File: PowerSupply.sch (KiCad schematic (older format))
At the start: 22 parts, among them IC1 TPS61252DSGT, J6 Conn_01x02, U1 LM27762

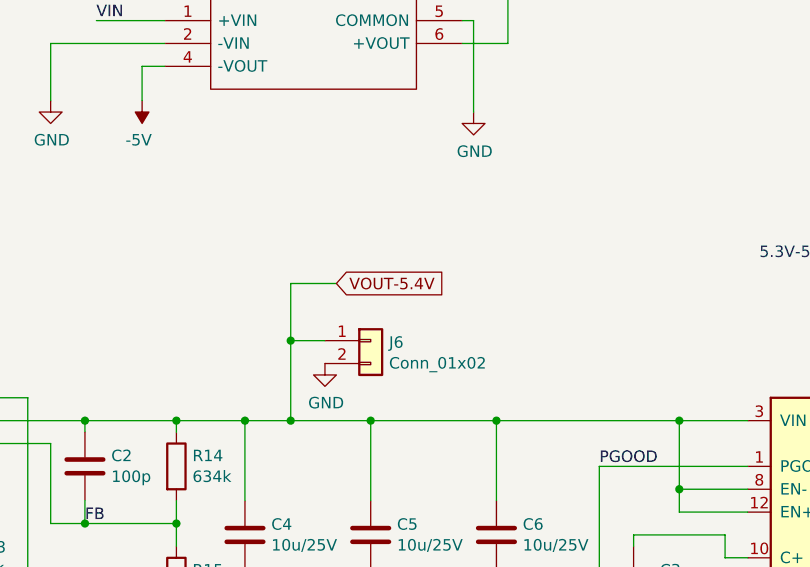
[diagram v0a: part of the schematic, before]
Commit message: larger conn
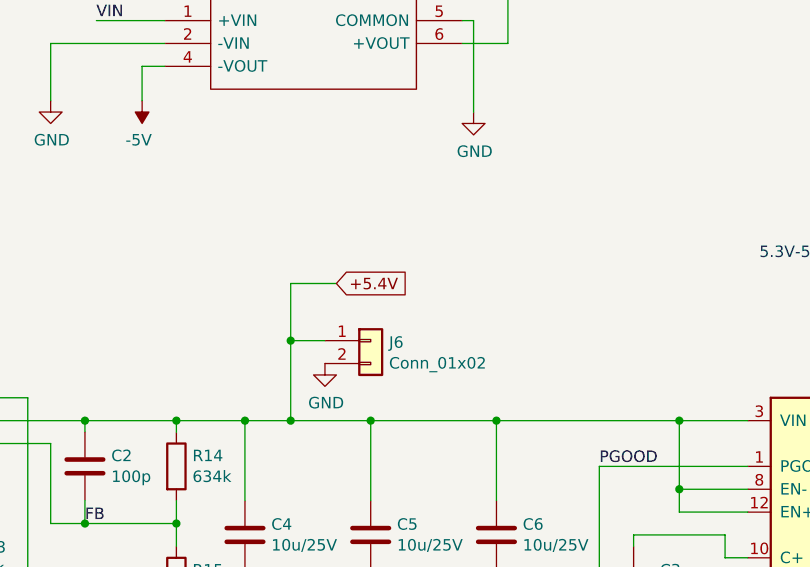
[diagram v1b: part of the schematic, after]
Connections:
- net VOUT-5.4V renamed +5.4V
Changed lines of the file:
@@
 FB
 Text GLabel 5350 2800 2    50   Input ~ 0
-VOUT-5.4V
++5.4V
 Wire Wire Line
 	5150 3050 5150 2800

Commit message: sch improv
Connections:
- net GND: now also U1.13 (PAD)
- net SW: now reaches IC1.7 (SW), L1.2
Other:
- note added: "Perhaps do not populate C27 and C5"
- moved on the sheet: L1
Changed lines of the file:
@@
 $EndComp
 Wire Wire Line
-	7550 4400 7550 4700
+	7550 4400 7550 4600
 $Comp
 L power:GND #PWR016
@@
 L Device:L L1
 U 1 1 5D3EB043
-P 2200 3400
-F 0 "L1" V 2000 3400 50  0000 C CNN
-F 1 "1.5u" V 2100 3400 50  0000 C CNN
-F 2 "BalancedAudioBox:SRN30151R5Y" H 2200 3400 50  0001 C CNN
-F 3 "~" H 2200 3400 50  0001 C CNN
-F 4 "SRN3015-1R5Y" V 2200 3400 50  0001 C CNN "PN"
-	1    2200 3400
+P 2100 3400
+F 0 "L1" V 1900 3400 50  0000 C CNN
+F 1 "1.5u" V 2000 3400 50  0000 C CNN
+F 2 "BalancedAudioBox:SRN30151R5Y" H 2100 3400 50  0001 C CNN
+F 3 "~" H 2100 3400 50  0001 C CNN
+F 4 "SRN3015-1R5Y" V 2100 3400 50  0001 C CNN "PN"
+	1    2100 3400
 	0    -1   -1   0
 $EndComp
 Wire Wire Line
-	2350 3400 2500 3400
+	2250 3400 2500 3400
 Wire Wire Line
 	2500 3300 2450 3300
@@
 	1900 3300 1900 3400
 Wire Wire Line
-	1900 3400 2050 3400
+	1900 3400 1950 3400
 Wire Wire Line
 	2500 3500 2450 3500
@@
 P 1700 4700
 F 0 "#PWR050" H 1700 4450 50  0001 C CNN
-F 1 "GND" H 1705 4527 50  0000 C CNN
+F 1 "GND" V 1705 4527 50  0000 C CNN
 F 2 "" H 1700 4700 50  0001 C CNN
 F 3 "" H 1700 4700 50  0001 C CNN
@@
 	5150 2800 5350 2800
 Connection ~ 5150 3050
+Text Notes 1450 5750 0    50   ~ 0
+Perhaps do not populate C27 and C5
+Text Label 2300 3400 0    50   ~ 0
+SW
+Wire Wire Line
+	7650 4400 7650 4600
+Wire Wire Line
+	7650 4600 7550 4600
+Connection ~ 7550 4600
+Wire Wire Line
+	7550 4600 7550 4700
 $EndSCHEMATC

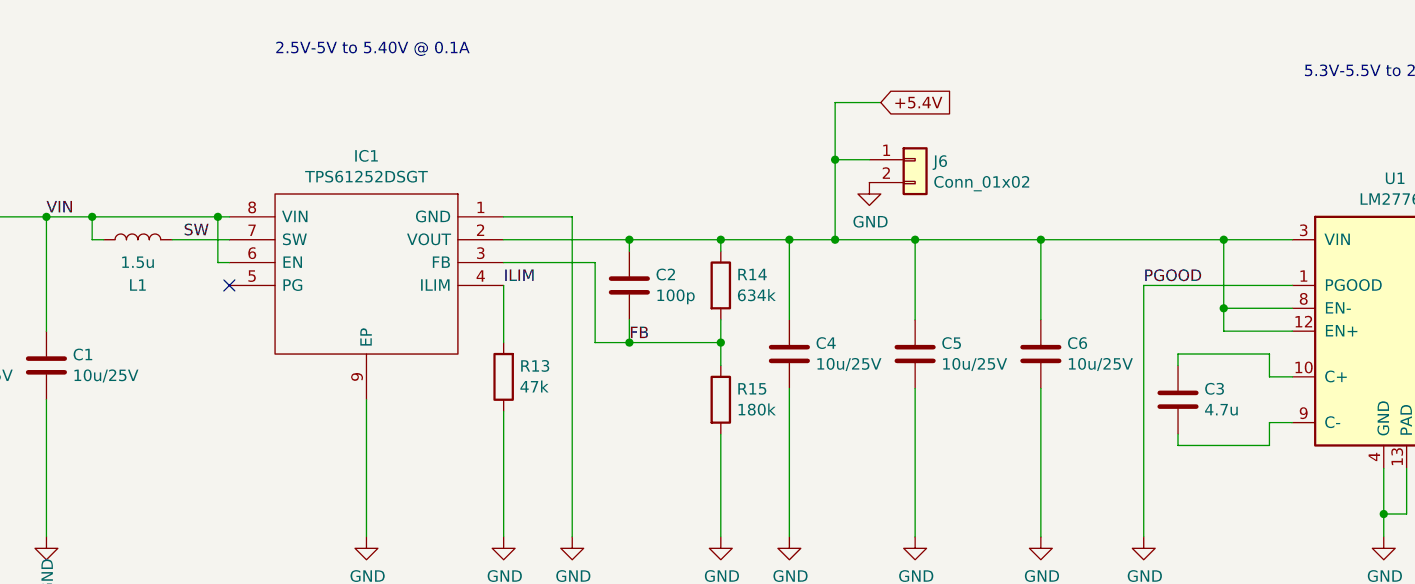
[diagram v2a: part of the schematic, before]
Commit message: smaller package, drc
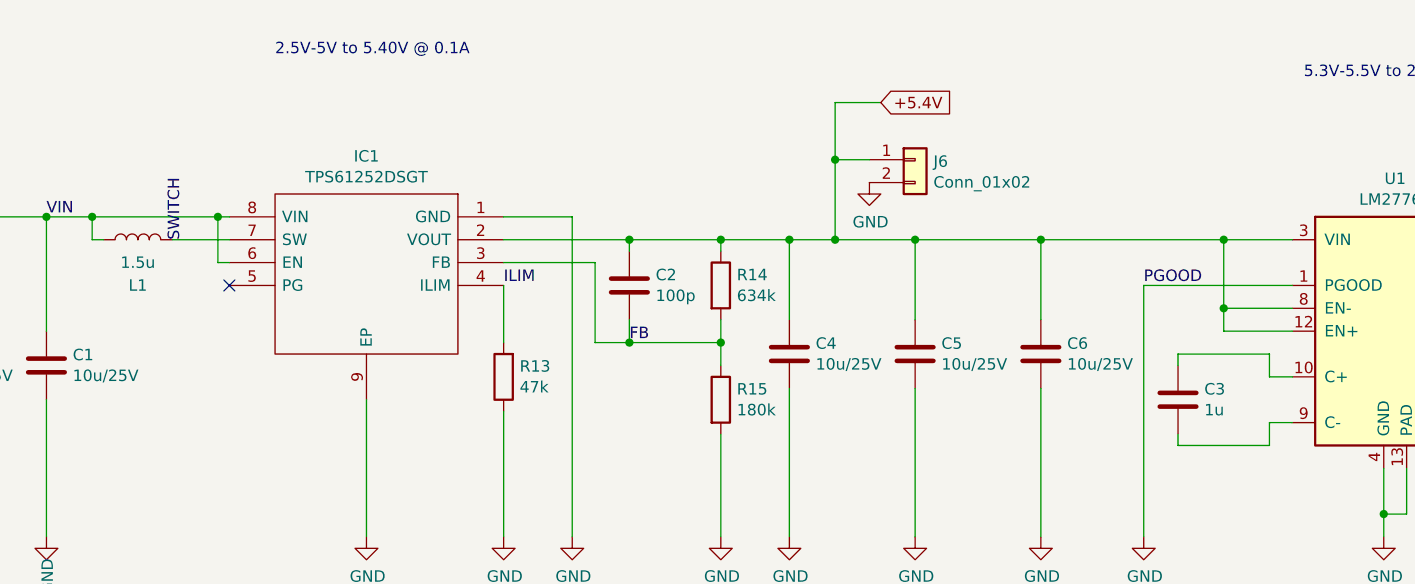
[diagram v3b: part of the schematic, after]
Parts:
- C21, C22: footprint Capacitor_SMD:C_0805_2012Metric -> Capacitor_SMD:C_0603_1608Metric
- C3: value 4.7u -> 1u; footprint Capacitor_SMD:C_0805_2012Metric -> Capacitor_SMD:C_0402_1005Metric
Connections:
- net SW renamed SWITCH
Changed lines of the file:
@@
 P 6650 4100
 F 0 "C3" H 6765 4146 50  0000 L CNN
-F 1 "4.7u" H 6765 4055 50  0000 L CNN
-F 2 "Capacitor_SMD:C_0805_2012Metric" H 6688 3950 50  0001 C CNN
+F 1 "1u" H 6765 4055 50  0000 L CNN
+F 2 "Capacitor_SMD:C_0402_1005Metric" H 6688 3950 50  0001 C CNN
 F 3 "~" H 6650 4100 50  0001 C CNN
 	1    6650 4100
@@
 	0    -1   -1   0
 $EndComp
-Wire Wire Line
-	2250 3400 2500 3400
 Wire Wire Line
 	2500 3300 2450 3300
@@
 F 0 "C21" H 8765 4546 50  0000 L CNN
 F 1 "4.7u" H 8765 4455 50  0000 L CNN
-F 2 "Capacitor_SMD:C_0805_2012Metric" H 8688 4350 50  0001 C CNN
+F 2 "Capacitor_SMD:C_0603_1608Metric" H 8688 4350 50  0001 C CNN
 F 3 "~" H 8650 4500 50  0001 C CNN
 	1    8650 4500
@@
 F 0 "C22" H 9415 4546 50  0000 L CNN
 F 1 "4.7u" H 9415 4455 50  0000 L CNN
-F 2 "Capacitor_SMD:C_0805_2012Metric" H 9338 4350 50  0001 C CNN
+F 2 "Capacitor_SMD:C_0603_1608Metric" H 9338 4350 50  0001 C CNN
 F 3 "~" H 9300 4500 50  0001 C CNN
 	1    9300 4500
@@
 Text Notes 1450 5750 0    50   ~ 0
 Perhaps do not populate C27 and C5
-Text Label 2300 3400 0    50   ~ 0
-SW
 Wire Wire Line
 	7650 4400 7650 4600
@@
 Wire Wire Line
 	7550 4600 7550 4700
+Wire Wire Line
+	2250 3400 2500 3400
+Text Label 2300 3400 1    50   ~ 0
+SWITCH
 $EndSCHEMATC
